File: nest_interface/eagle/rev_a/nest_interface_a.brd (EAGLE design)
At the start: 114.3 x 83.8 mm, 98 parts, among them J1 MOLEX_MICRO_USB_B_047346, J10 CONN_BLOCK_2, J11 CONN_BLOCK_2, J12 CONN_BLOCK_2, J13 CONN_BLOCK_2, J14 CONN_BLOCK_2, J15 CONN_BLOCK_2, J16 CONN_BLOCK_2, J17 CONN_BLOCK_3, J2 CONN_BLOCK_2, J3 CONN_BLOCK_3, J4 PJ-036A-SMT, J5 CONN_BLOCK_3, J6 CONN_BLOCK_3, J7 CONN_BLOCK_2, J8 CONN_BLOCK_3, J9 CONN_BLOCK_3, U1 FT232RL, U2 EPIC-CORE_A, U3 MPC1825

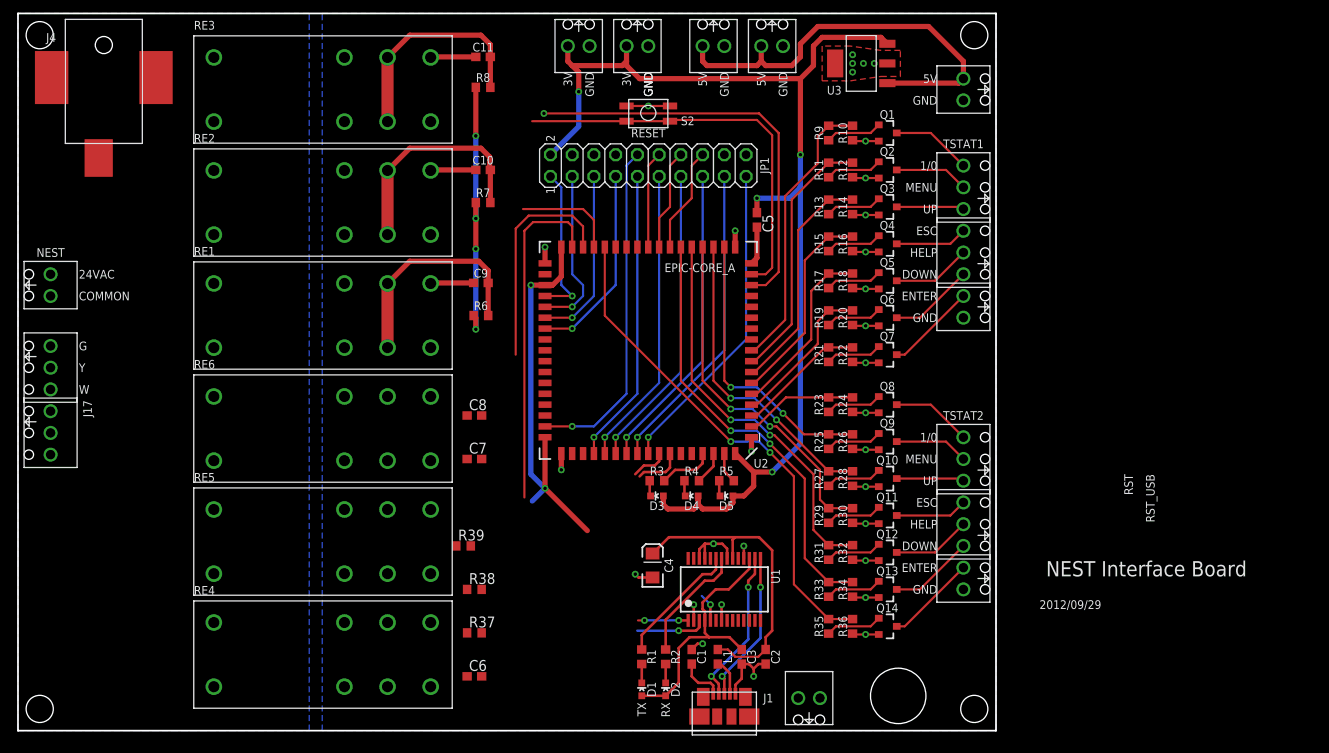
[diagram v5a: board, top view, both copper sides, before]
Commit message: added relays
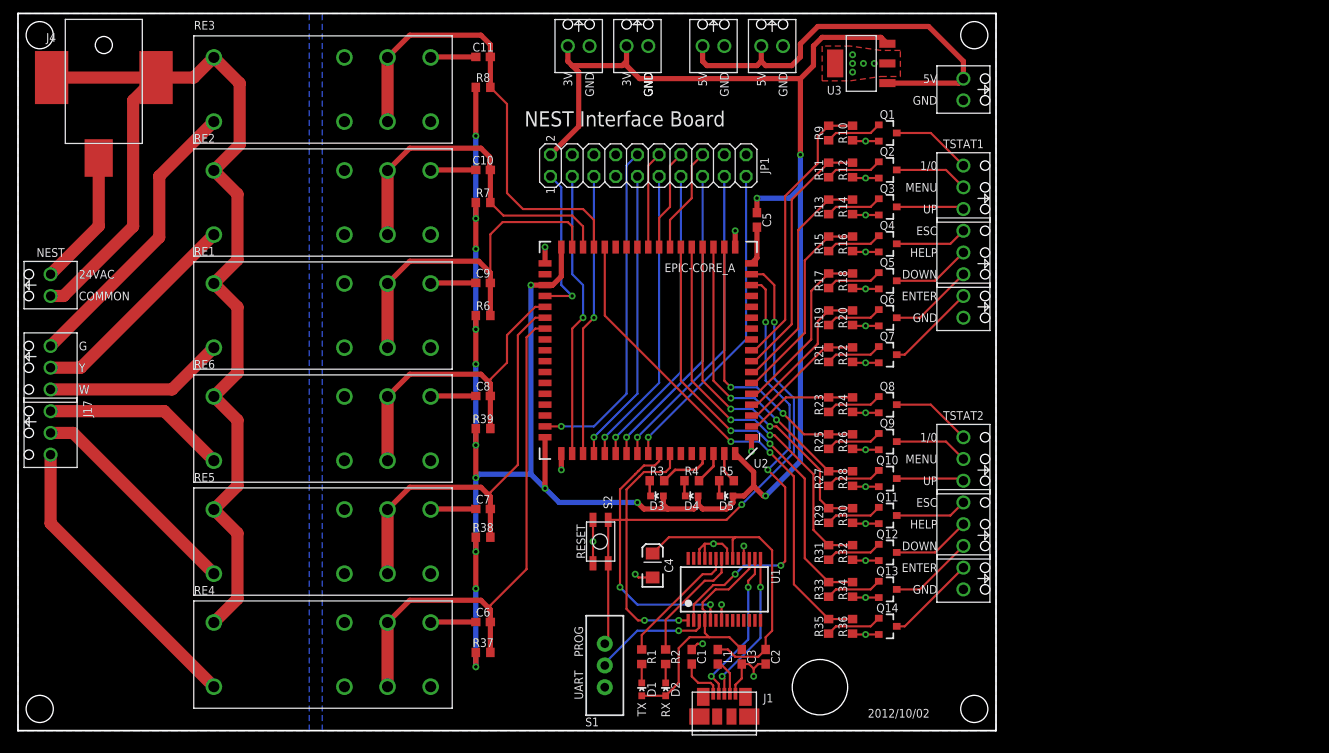
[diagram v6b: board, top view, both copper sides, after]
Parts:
- removed J16: CONN_BLOCK_2, nest_interface:CONN_BLOCK_2
- added S1: (no value), SparkFun:SWITCH-SPDT
- moved S2 50.3 mm to (68.1, 22.1), turned to 270 degrees
- moved R39 13.9 mm to (54.4, 35.3), turned to 180 degrees
- moved C6 6.43 mm to (54.4, 12.7), turned to 180 degrees
- moved R38 6.18 mm to (54.4, 22.6), turned to 180 degrees
- moved C7 5.93 mm to (54.4, 25.9), turned to 180 degrees
- moved C8 2.50 mm to (54.4, 39.1), turned to 180 degrees
- moved R37 2.50 mm to (54.4, 9.14), turned to 180 degrees
- moved C9 0.25 mm to (54.4, 52.3)
- moved R6 0.25 mm to (54.4, 48.5)
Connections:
- removed net P2.1: JP1.3, U2.P$39
- removed net P2.3: JP1.5, U2.P$40
- removed net P2.6: JP1.7, U2.P$41
- new net P2.4: JP1.5, U2.P$54
- new net P2.7: JP1.3, U2.P$53
- net COOLING2_PIN: now also U2.P$40
- net HEATING2_PIN: now also U2.P$41
- net RST: now also S1.1; no longer J16.1
- net RST_USB: now also S1.2; no longer J16.2
- net STAR_PIN: now also U2.P$39
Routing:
- net COMMON: track 0.00 -> 129.2 mm
- net HEATING2_PIN: track 0.00 -> 62.4 mm
- net VCC: track 213.2 -> 273.6 mm, vias 10 -> 16
- net COOLING2_PIN: track 0.00 -> 50.0 mm
- net STAR_PIN: track 0.00 -> 38.6 mm
- net W2: track 0.00 -> 35.0 mm
- net G: track 0.00 -> 34.1 mm
- net P2.7: track 0.00 -> 33.4 mm, vias 0 -> 1
- net P2.4: track 0.00 -> 32.9 mm, vias 0 -> 1
- net Y2: track 0.00 -> 25.9 mm
- net Y1: track 0.00 -> 25.5 mm
- net N$12: track 7.60 -> 31.5 mm, vias 1 -> 2
- net P2.6: track 23.1 -> 0.00 mm, vias 1 -> 0
- net HEATING1_PIN: track 65.8 -> 43.6 mm
- net STAR: track 0.00 -> 21.5 mm
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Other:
- board text added: "2012/10/02"
- board text added: "PROG"
- board text added: "UART"
- board text removed: "2012/09/29"
- board text removed: "RST"
- board text removed: "RST_USB"

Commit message: BETTER NEST
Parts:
- added R40, R41, R42, R43, R44, R45, R46, R47, R48, R49, R50, R51, R52, R53, R54, R55, R56, R57, R58, R59, R60, R61, R62, R63, R64, R65, R68, R69: 100k, rcl:R0603
- added R66, R67: 0, rcl:R0603
- added R70, R71: 10k, rcl:R0603
- added U$1, U$2, U$3, U$4: ALD1107, nest_interface:SOIC-14
- added U4, U5: PCA9575, nest_interface:TSSOP28
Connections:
- removed net TSTAT1_DOWN_PIN: R19.2, R20.1, U2.P$4
- removed net TSTAT1_ENTER_PIN: R21.2, R22.1, U2.P$3
- removed net TSTAT1_ESC_PIN: R15.2, R16.1, U2.P$6
- removed net TSTAT1_HELP_PIN: R17.2, R18.1, U2.P$5
- removed net TSTAT1_MENU_PIN: R11.2, R12.1, U2.P$8
- removed net TSTAT1_ON/OFF_PIN: R10.1, R9.2, U2.P$9
- removed net TSTAT1_UP_PIN: R13.2, R14.1, U2.P$7
- removed net TSTAT2_DOWN_PIN: R33.2, R34.1, U2.P$23
- removed net TSTAT2_ENTER_PIN: R35.2, R36.1, U2.P$30
- removed net TSTAT2_ESC_PIN: R29.2, R30.1, U2.P$21
- removed net TSTAT2_HELP_PIN: R31.2, R32.1, U2.P$22
- removed net TSTAT2_MENU_PIN: R25.2, R26.1, U2.P$19
- removed net TSTAT2_ON/OFF_PIN: R23.2, R24.1, U2.P$2
- removed net TSTAT2_UP_PIN: R27.2, R28.1, U2.P$20
- new net #KEYPAD_ENABLE: R40.2, R41.2, R42.2, R43.2, R48.2, R49.2, R50.2, R51.2, R56.2, R57.2, R58.2, R59.2, R64.2, R65.2, U$1.13, U$1.2, U$1.6, U$1.9, U$2.13, U$2.2, U$2.6, U$2.9, U$3.13, U$3.2, U$3.6, U$3.9, U$4.13, U$4.2
- new net I2C_SCL: R70.1, U2.P$58, U4.28, U5.28
- new net I2C_SDA: R71.1, U2.P$56, U4.27, U5.27
- new net N$37: R66.2, U4.3
- new net N$58: R67.2, U5.3
- new net TSTAT1_DOWN_IN: R53.1, U$2.12, U4.11
- new net TSTAT1_DOWN_OUT: Q6.3, U$2.14
- new net TSTAT1_DOWN_OUT_PIN: R19.2, R20.1, U5.11
- new net TSTAT1_ENTER_IN: R54.1, U$2.8, U4.12
- new net TSTAT1_ENTER_OUT: Q7.3, U$2.10
- new net TSTAT1_ENTER_OUT_PIN: R21.2, R22.1, U5.12
- new net TSTAT1_ESC_IN: R47.1, U$1.7, U4.7
- new net TSTAT1_ESC_OUT: Q4.3, U$1.5
- new net TSTAT1_ESC_OUT_PIN: R15.2, R16.1, U5.7
- new net TSTAT1_HELP_IN: R52.1, U$2.3, U4.10
- new net TSTAT1_HELP_OUT: Q5.3, U$2.1
- new net TSTAT1_HELP_OUT_PIN: R17.2, R18.1, U5.10
- new net TSTAT1_MENU_IN: R45.1, U$1.12, U4.5
- new net TSTAT1_MENU_OUT: Q2.3, U$1.14
- new net TSTAT1_MENU_OUT_PIN: R11.2, R12.1, U5.5
- new net TSTAT1_ON/OFF_IN: R44.1, U$1.3, U4.4
- new net TSTAT1_ON/OFF_OUT: Q1.3, U$1.1
- new net TSTAT1_ON/OFF_OUT_PIN: R10.1, R9.2, U5.4
- new net TSTAT1_UP_IN: R46.1, U$1.8, U4.6
- new net TSTAT1_UP_OUT: Q3.3, U$1.10
- new net TSTAT1_UP_OUT_PIN: R13.2, R14.1, U5.6
- new net TSTAT2_DOWN_IN: R68.1, U$4.3, U4.19
- new net TSTAT2_DOWN_OUT: Q13.3, U$4.1
- new net TSTAT2_DOWN_OUT_PIN: R33.2, R34.1, U5.19
- new net TSTAT2_ENTER_IN: R69.1, U$4.12, U4.18
- new net TSTAT2_ENTER_OUT: Q14.3, U$4.14
- new net TSTAT2_ENTER_OUT_PIN: R35.2, R36.1, U5.18
- new net TSTAT2_ESC_IN: R62.1, U$3.8, U4.23
- new net TSTAT2_ESC_OUT: Q11.3, U$3.10
- new net TSTAT2_ESC_OUT_PIN: R29.2, R30.1, U5.23
- new net TSTAT2_HELP_IN: R63.1, U$3.7, U4.20
- new net TSTAT2_HELP_OUT: Q12.3, U$3.5
- new net TSTAT2_HELP_OUT_PIN: R31.2, R32.1, U5.20
- new net TSTAT2_MENU_IN: R60.1, U$3.3, U4.25
- new net TSTAT2_MENU_OUT: Q9.3, U$3.1
- new net TSTAT2_MENU_OUT_PIN: R25.2, R26.1, U5.25
- new net TSTAT2_ON/OFF_IN: R55.1, U$2.7, U4.26
- new net TSTAT2_ON/OFF_OUT: Q8.3, U$2.5
- new net TSTAT2_ON/OFF_OUT_PIN: R23.2, R24.1, U5.26
- new net TSTAT2_UP_IN: R61.1, U$3.12, U4.24
- new net TSTAT2_UP_OUT: Q10.3, U$3.14
- new net TSTAT2_UP_OUT_PIN: R27.2, R28.1, U5.24
- new net TSTAT_IN_I2C_INT: U4.14
- new net TSTAT_OUT_I2C_INT: U5.14
- net GND: now also R40.1, R41.1, R42.1, R43.1, R48.1, R49.1, R50.1, R51.1, R56.1, R57.1, R58.1, R59.1, R64.1, R65.1, U$1.4, U$2.4, U$3.4, U$4.4, U4.13, U4.16, U4.17, U4.22, U5.13, U5.15, U5.16, U5.17, U5.22
- net MOSI0/SDA: no longer U2.P$56
- net SCLK0/SCL: no longer U2.P$58
- net TSTAT1_DOWN: no longer Q6.3
- net TSTAT1_ENTER: no longer Q7.3
- net TSTAT1_ESC: no longer Q4.3
- net TSTAT1_HELP: no longer Q5.3
- net TSTAT1_MENU: no longer Q2.3
- net TSTAT1_ON/OFF: no longer Q1.3
- net TSTAT1_UP: no longer Q3.3
- net TSTAT2_DOWN: no longer Q13.3
- net TSTAT2_ENTER: no longer Q14.3
- net TSTAT2_ESC: no longer Q11.3
- net TSTAT2_HELP: no longer Q12.3
- net TSTAT2_MENU: no longer Q9.3
- net TSTAT2_ON/OFF: no longer Q8.3
- net TSTAT2_UP: no longer Q10.3
- net VCC: now also R44.2, R45.2, R46.2, R47.2, R52.2, R53.2, R54.2, R55.2, R60.2, R61.2, R62.2, R63.2, R66.1, R67.1, R68.2, R69.2, R70.2, R71.2, U$1.11, U$2.11, U$3.11, U$4.11, U4.1, U4.15, U4.2, U4.21, U4.8, U4.9, U5.1, U5.2, U5.21, U5.8, U5.9
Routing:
- net TSTAT2_ENTER_PIN: track 59.0 -> 0.00 mm, vias 2 -> 0
- net TSTAT2_DOWN_PIN: track 50.9 -> 0.00 mm, vias 2 -> 0
- net TSTAT2_HELP_PIN: track 46.2 -> 0.00 mm, vias 2 -> 0
- net TSTAT2_ESC_PIN: track 41.3 -> 0.00 mm, vias 2 -> 0
- net TSTAT2_UP_PIN: track 36.3 -> 0.00 mm, vias 2 -> 0
- net W2: track 35.0 -> 0.00 mm
- net TSTAT2_MENU_PIN: track 33.2 -> 0.00 mm, vias 2 -> 0
- net TSTAT1_ON/OFF_PIN: track 33.0 -> 0.00 mm
- net TSTAT1_MENU_PIN: track 30.0 -> 0.00 mm
- net TSTAT1_UP_PIN: track 26.9 -> 0.00 mm
- net Y2: track 25.9 -> 0.00 mm
- net TSTAT1_ESC_PIN: track 23.9 -> 0.00 mm
- net STAR: track 21.5 -> 0.00 mm
- net TSTAT1_HELP_PIN: track 21.0 -> 0.00 mm
- net TSTAT1_DOWN_PIN: track 17.9 -> 0.00 mm
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- added copper zone on layer 16, net #KEYPAD_ENABLE
- removed copper zone on layer 16, net N$37

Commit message: saving nest i board
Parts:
- added C12, C13, C14, C17: 0.1u, rcl:C0603
- added C15: 10u, SparkFun:EIA3216
- added C16: 1u, rcl:C0603
- added D10, D6, D7, D8, D9: (no value), SparkFun:LED-0603
- added J16, J19, J20, J21, J23, J24: CONN_BLOCK_3, nest_interface:CONN_BLOCK_3
- added J18, J22: CONN_BLOCK_2, nest_interface:CONN_BLOCK_2
- added J25: MOLEX_MICRO_USB_B_047346, nest_interface:MOLEX_MICRO_USB_B_047346
- added L2: (no value), SparkFun:0603
- added R72, R77: 100k, rcl:R0603
- added R73, R74, R78, R79, R80: 240, rcl:R0603
- added R75: 5.1M, rcl:R0603
- added R76: 100k 0.1%, rcl:R0603
- added RA1, RA2, RA3, RA4: VSSR2403103, nest_interface:LSSOP-24
- added S3: EVQP2, berkeley-epic:EVQP2
- added S4: (no value), SparkFun:SWITCH-SPDT
- added U$5: MSP430F1611IPM, hijack:PM/PAG64
- added U6: FT232RL, ftdichip:SSOP28
- added Y1: FC-135_32.768KA-A3, berkeley-epic:FC-135
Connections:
- removed net TSTAT_OUT_I2C_INT: U5.14
- new net N$13: D8.C, R78.2
- new net N$38: U$5.8, Y1.1
- new net N$39: C12.1, J25.VCC
- new net N$40: J25.D-, U6.16
- new net N$41: J25.D+, U6.15
- new net N$42: J25.ID, L2.1
- new net N$43: C13.1, C15.A, L2.2, U6.20
- new net N$44: R73.1, U6.23
- new net N$45: R74.1, U6.22
- new net N$46: D6.C, R73.2
- new net N$47: D7.C, R74.2
- new net N$48: U$5.34, U6.1
- new net N$49: U6.5
- new net N$50: U$5.57, U6.2
- new net N$51: C14.1, D6.A, D7.A, U6.17, U6.4
- new net N$52: R75.2, U$5.9, Y1.2
- new net N$53: D9.C, R79.2
- new net N$54: R76.2, U$5.25
- new net N$55: D10.C, R80.2
- new net N$56: R79.1, U$5.21
- new net N$57: R80.1, U$5.22
- new net N$8: R78.1, U$5.20
- new net RST1: C17.1, R77.2, S3.P$2, S3.P$4, S4.1, U$5.58
- new net RST_USB1: S4.2, U6.3
- new net TSTAT1_LCD_DB0: J19.1, RA1.7
- new net TSTAT1_LCD_DB0_PIN: RA1.17, RA1.18, U$5.36
- new net TSTAT1_LCD_DB1: J19.2, RA1.9
- new net TSTAT1_LCD_DB1_PIN: RA1.15, RA1.16, U$5.37
- new net TSTAT1_LCD_DB2: J19.3, RA1.11
- new net TSTAT1_LCD_DB2_PIN: RA1.13, RA1.14, U$5.38
- new net TSTAT1_LCD_DB3: J20.1, RA2.1
- new net TSTAT1_LCD_DB3_PIN: RA2.23, RA2.24, U$5.39
- new net TSTAT1_LCD_DB4: J20.2, RA2.3
- new net TSTAT1_LCD_DB4_PIN: RA2.21, RA2.22, U$5.40
- new net TSTAT1_LCD_DB5: J20.3, RA2.5
- new net TSTAT1_LCD_DB5_PIN: RA2.19, RA2.20, U$5.41
- new net TSTAT1_LCD_DB6: J18.1, RA2.7
- new net TSTAT1_LCD_DB6_PIN: RA2.17, RA2.18, U$5.42
- new net TSTAT1_LCD_DB7: J18.2, RA2.9
- new net TSTAT1_LCD_DB7_PIN: RA2.15, RA2.16, U$5.43
- new net TSTAT1_LCD_E: J16.3, RA1.5
- new net TSTAT1_LCD_E_PIN: RA1.19, RA1.20, U$5.14
- new net TSTAT1_LCD_R/W: J16.2, RA1.3
- new net TSTAT1_LCD_R/W_PIN: RA1.21, RA1.22, U$5.13
- new net TSTAT1_LCD_RS: J16.1, RA1.1
- new net TSTAT1_LCD_RS_PIN: RA1.23, RA1.24, U$5.12
- new net TSTAT2_LCD_DB0: J23.1, RA3.7
- new net TSTAT2_LCD_DB0_PIN: RA3.17, RA3.18, U$5.59
- new net TSTAT2_LCD_DB1: J23.2, RA3.9
- new net TSTAT2_LCD_DB1_PIN: RA3.15, RA3.16, U$5.60
- new net TSTAT2_LCD_DB2: J23.3, RA3.11
- new net TSTAT2_LCD_DB2_PIN: RA3.13, RA3.14, U$5.61
- new net TSTAT2_LCD_DB3: J24.1, RA4.1
- new net TSTAT2_LCD_DB3_PIN: RA4.23, RA4.24, U$5.2
- new net TSTAT2_LCD_DB4: J24.2, RA4.3
- new net TSTAT2_LCD_DB4_PIN: RA4.21, RA4.22, U$5.3
- new net TSTAT2_LCD_DB5: J24.3, RA4.5
- new net TSTAT2_LCD_DB5_PIN: RA4.19, RA4.20, U$5.4
- new net TSTAT2_LCD_DB6: J22.1, RA4.7
- new net TSTAT2_LCD_DB6_PIN: RA4.17, RA4.18, U$5.5
- new net TSTAT2_LCD_DB7: J22.2, RA4.9
- new net TSTAT2_LCD_DB7_PIN: RA4.15, RA4.16, U$5.6
- new net TSTAT2_LCD_E: J21.3, RA3.5
- new net TSTAT2_LCD_E_PIN: RA3.19, RA3.20, U$5.17
- new net TSTAT2_LCD_R/W: J21.2, RA3.3
- new net TSTAT2_LCD_R/W_PIN: RA3.21, RA3.22, U$5.16
- new net TSTAT2_LCD_RS: J21.1, RA3.1
- new net TSTAT2_LCD_RS_PIN: RA3.23, RA3.24, U$5.15
- net GND: now also C12.2, C13.2, C14.2, C15.C, C16.2, C17.2, J25.GND, R75.1, RA1.10, RA1.12, RA1.2, RA1.4, RA1.6, RA1.8, RA2.10, RA2.2, RA2.4, RA2.6, RA2.8, RA3.10, RA3.12, RA3.2, RA3.4, RA3.6, RA3.8, RA4.10, RA4.2, RA4.4, RA4.6, RA4.8, S3.P$1, S3.P$3, U$5.10, U$5.11, U$5.53, U$5.62, U$5.63, U6.18, U6.21, U6.25, U6.26, U6.7; no longer U5.13, U5.17
- net I2C_SCL: now also U$5.31
- net I2C_SDA: now also U$5.29
- net TSTAT_IN_I2C_INT: now also R72.2
- net VCC: now also C16.1, D10.A, D8.A, D9.A, R72.1, R76.1, R77.1, U$5.1, U$5.64
